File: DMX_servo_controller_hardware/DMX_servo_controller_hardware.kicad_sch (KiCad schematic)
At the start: 43 parts, among them J1 Power connector, J10 Conn_01x03, J11 Conn_01x03, J12 Conn_01x03, J2 XLR, J3 Display, J4 Rotary encoder, J5 Conn_01x03, J6 Conn_01x03, J7 Conn_01x03, J8 Conn_01x03, J9 Conn_01x03, SW1 Reset, U1 PCA9685PW, U2 SN65HVD11HD, U3 6N137, U4 Pico

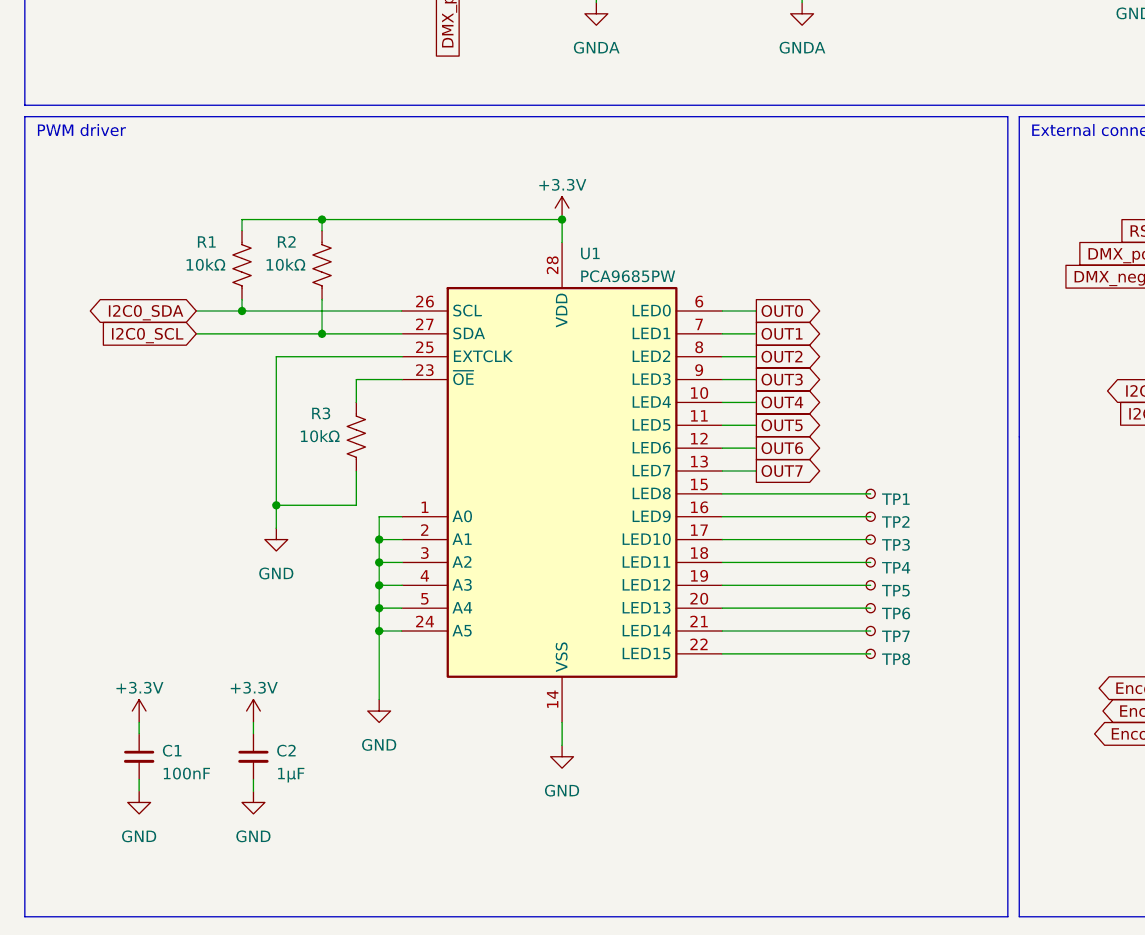
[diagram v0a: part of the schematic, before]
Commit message: Powers PCA9685 from 5V rail
With this, the PWM signal will be on the level the servos expect, since
they will be powered with the same voltage. The i2c lines are level
shifted since the RP2040 GPIOs are not 5V tolerant.
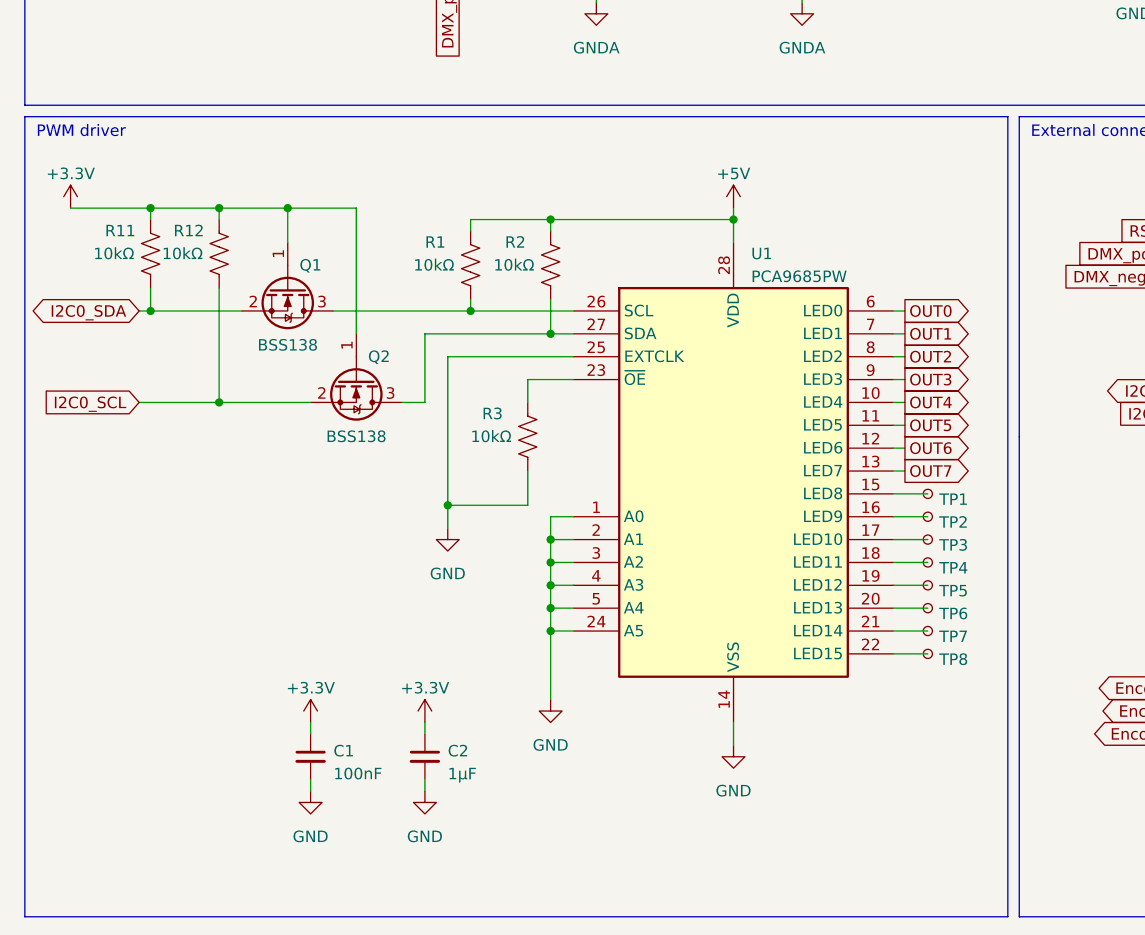
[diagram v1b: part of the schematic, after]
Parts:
- added Q1, Q2: BSS138, Package_TO_SOT_SMD:SOT-23, symbol Transistor_FET:BSS138
- added R11, R12: 10kΩ, symbol Device:R_US
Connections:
- net +3.3V: now also Q1.1 (G), Q2.1 (G), R11.1, R12.1; no longer R1.1, R2.1, U1.28 (VDD)
- net +5V: now also R1.1, R2.1, U1.28 (VDD)
- net I2C0_SCL: now also Q2.2 (S), R12.2; no longer R2.2, U1.27 (SDA)
- net I2C0_SDA: now also Q1.2 (S), R11.2; no longer R1.2, U1.26 (SCL)
- new net: Q1.3 (D), R1.2, U1.26 (SCL)
- new net: Q2.3 (D), R2.2, U1.27 (SDA)
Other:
- moved on the sheet: C1, C2, R1, R2, R3, TP1, TP2, TP3, TP4, TP5, TP6, TP7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

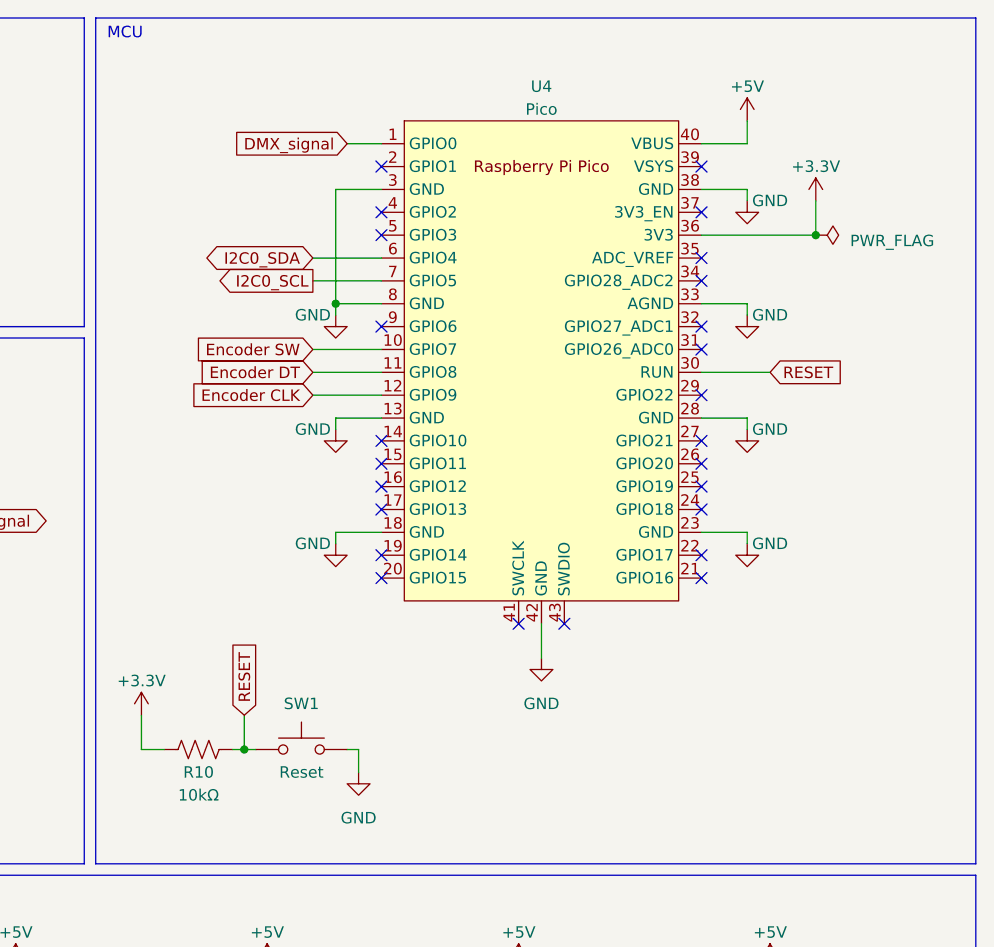
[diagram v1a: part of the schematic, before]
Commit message: Adds a diode to stop the USB from feeding the power supply when programming
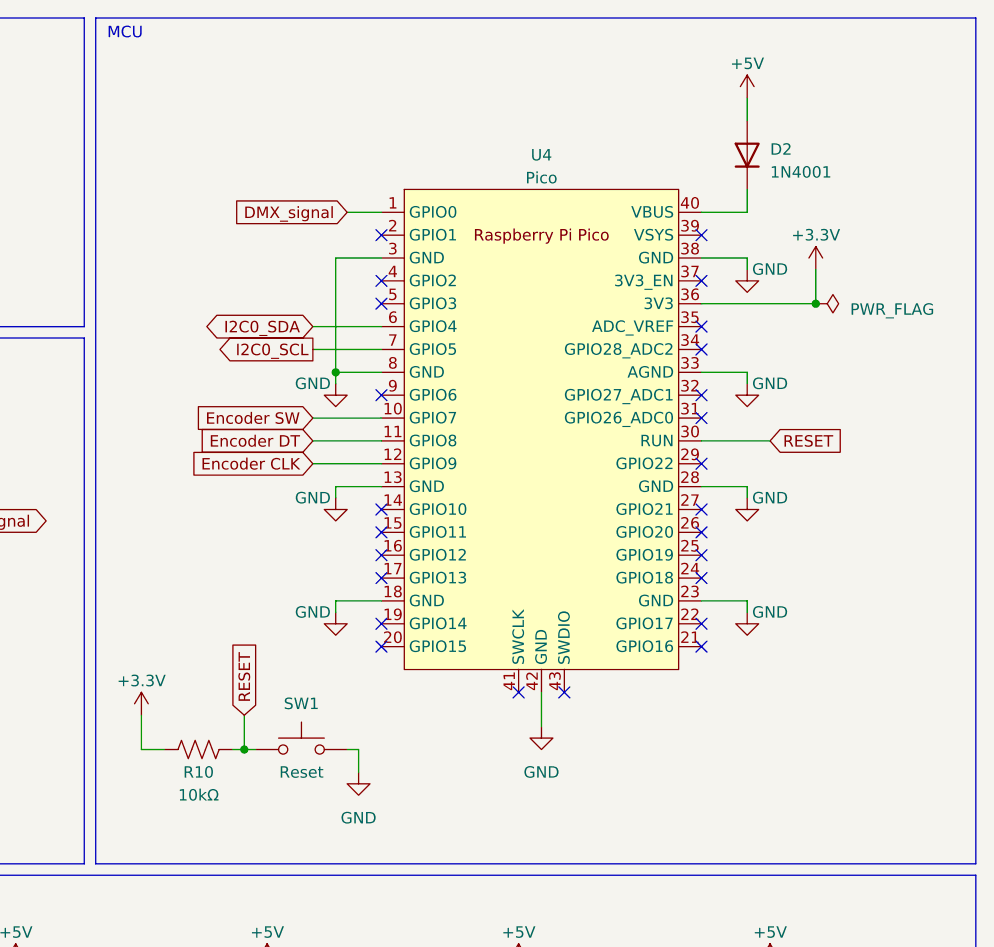
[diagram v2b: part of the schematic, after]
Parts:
- added D2: 1N4001, Diode_THT:D_DO-41_SOD81_P10.16mm_Horizontal, symbol Diode:1N4001
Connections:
- net +5V: now also D2.2 (A); no longer U4.40 (VBUS)
- new net: D2.1 (K), U4.40 (VBUS)
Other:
- moved on the sheet: U4

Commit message: Reasigns component designators
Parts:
- renumbered D2 to D1, R11 to R1, R8 to R10, R9 to R11, R10 to R12, R12 to R2, R1 to R3, R3 to R6, R2 to R7, R6 to R8, R7 to R9

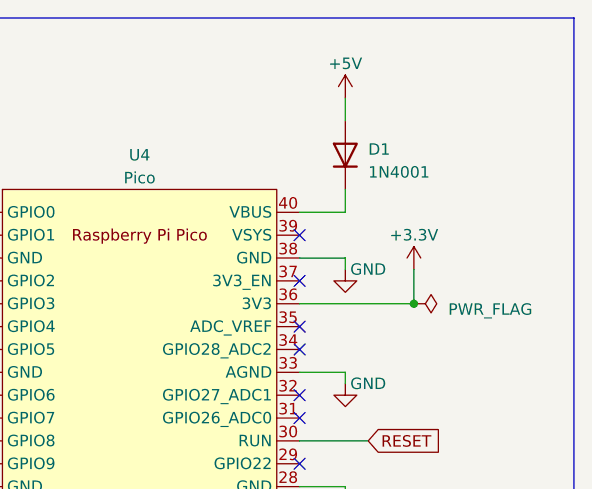
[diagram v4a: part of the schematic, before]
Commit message: Adds power flag to the VUSB net after the diode
This is necessary so the ERC will not complain about the pin do being
driven.
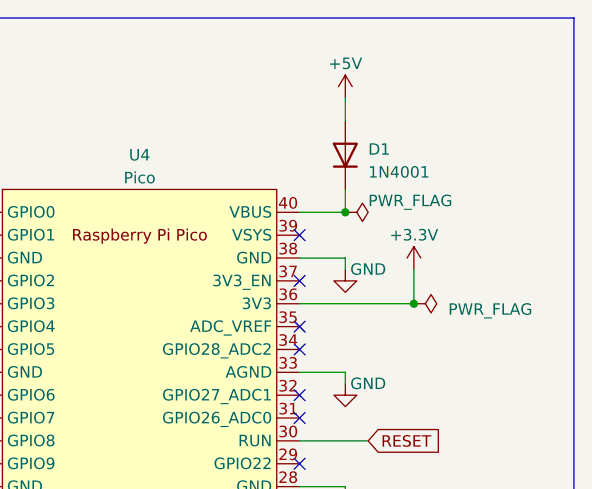
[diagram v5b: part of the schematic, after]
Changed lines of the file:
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@@
   (junction (at 71.12 160.02) (diameter 0) (color 0 0 0 0)
+  )
+  (junction (at 259.08 34.29) (diameter 0) (color 0 0 0 0)
   )
   (junction (at 62.23 129.54) (diameter 0) (color 0 0 0 0)
@@
         )
       )
+    )
+  )
+  (symbol (lib_id "power:PWR_FLAG") (at 259.08 34.29 270) (unit 1)
+    (in_bom yes) (on_board yes) (dnp no)
+    (property "Reference" "#FLG04" (at 260.985 34.29 0)
+      (effects (font (size 1.27 1.27)) hide)
+    )
+    (property "Value" "PWR_FLAG" (at 261.62 33.02 90)
+      (effects (font (size 1.27 1.27)) (justify left))
+    )
+    (property "Footprint" "" (at 259.08 34.29 0)
+      (effects (font (size 1.27 1.27)) hide)
+    )
+    (property "Datasheet" "~" (at 259.08 34.29 0)
+      (effects (font (size 1.27 1.27)) hide)
+    )
+    (pin "1")
+    (instances
+      (project "DMX_servo_controller_hardware"
+        (path "/cd90393c-7fb4-4867-84b8-7df1a2bf6613"
+          (reference "#FLG04") (unit 1)
+        )
+      )

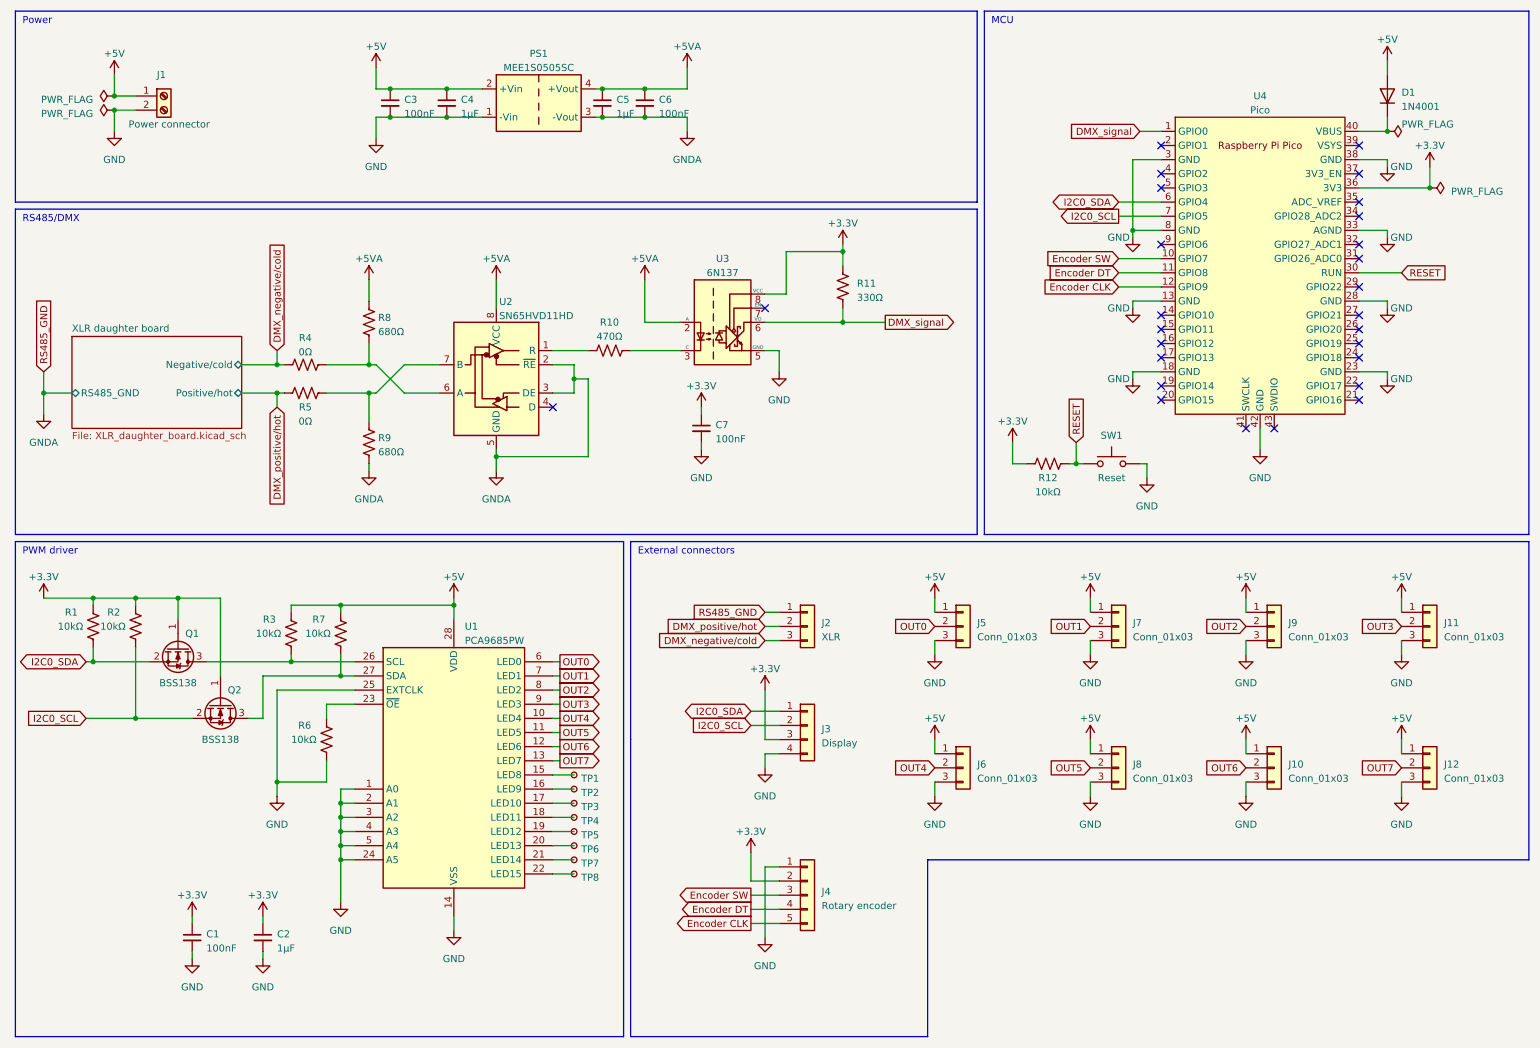
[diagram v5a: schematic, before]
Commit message: Final review of the schematics
* Fixes SCL pull-up in PCA9685
* Reviews pinouts
* Adds series resistor to PWM signals
* Adds bulk decoupling capacitor to 5V power rail
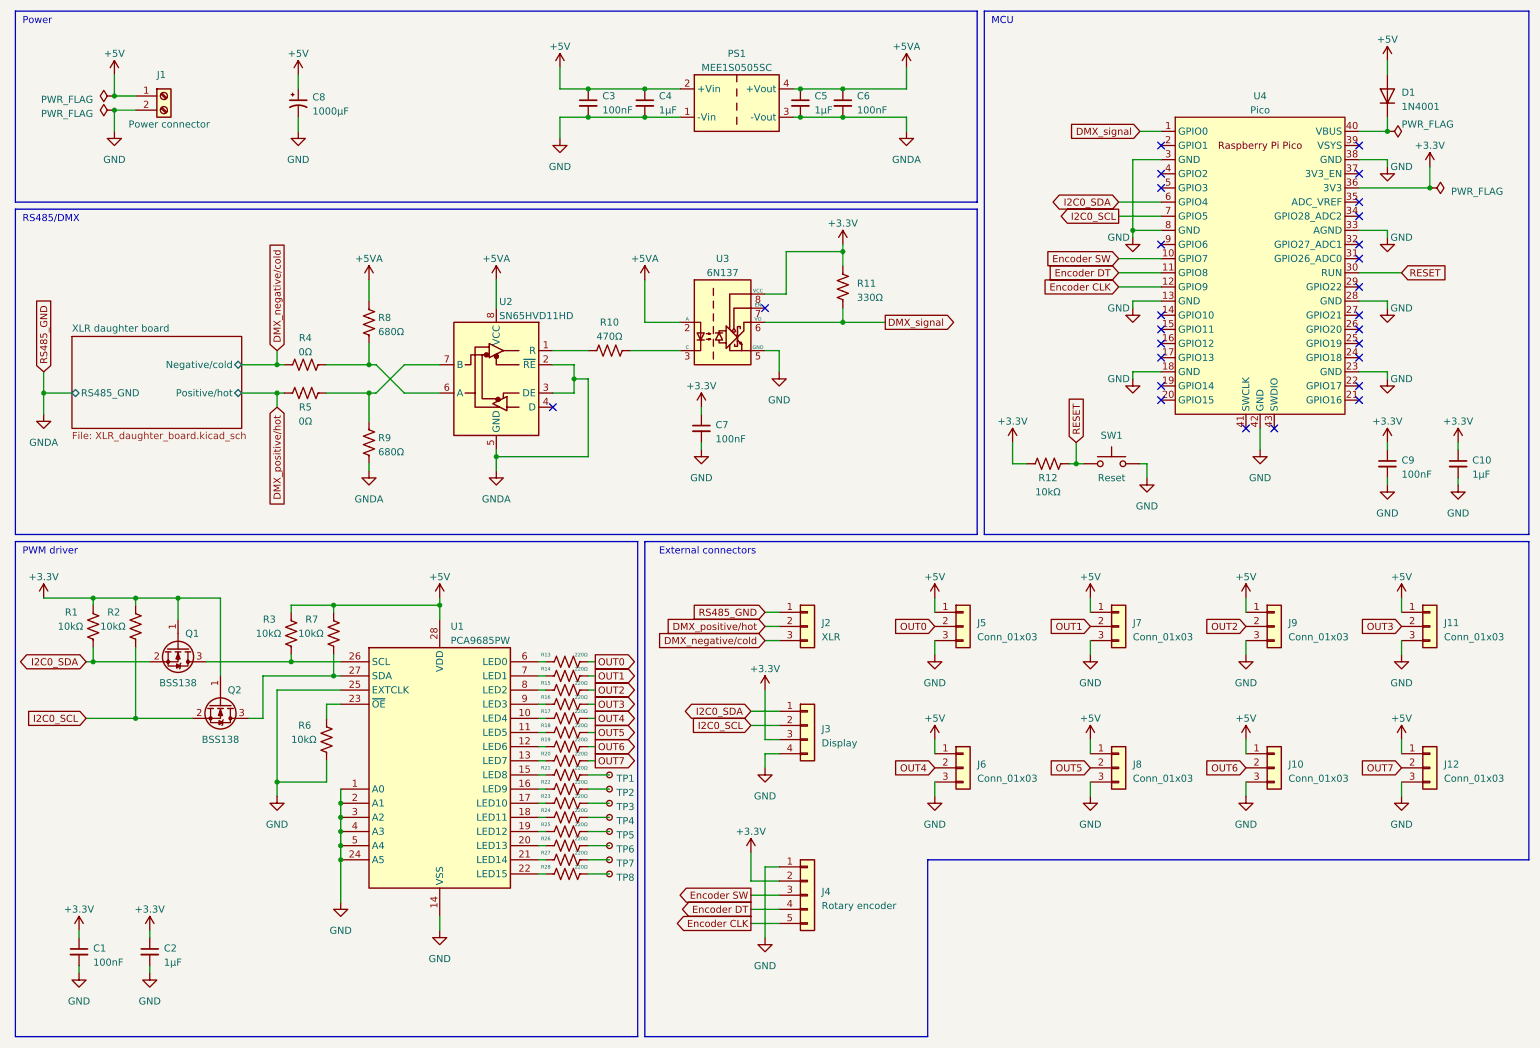
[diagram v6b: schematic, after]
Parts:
- added C10: 1μF, symbol Device:C_Small
- added C8: 1000μF, symbol Device:C_Polarized_Small_US
- added C9: 100nF, symbol Device:C_Small
- added R13, R14, R15, R16, R17, R18, R19, R20, R21, R22, R23, R24, R25, R26, R27, R28: 220Ω, symbol Device:R_US
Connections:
- net +3.3V: now also C10.1, C9.1
- net +5V: now also C8.1
- net GND: now also C10.2, C8.2, C9.2
- net OUT0: now also R13.2; no longer U1.6 (LED0)
- net OUT1: now also R14.2; no longer U1.7 (LED1)
- net OUT2: now also R15.2; no longer U1.8 (LED2)
- net OUT3: now also R16.2; no longer U1.9 (LED3)
- net OUT4: now also R17.2; no longer U1.10 (LED4)
- net OUT5: now also R18.2; no longer U1.11 (LED5)
- net OUT6: now also R19.2; no longer U1.12 (LED6)
- net OUT7: now also R20.2; no longer U1.13 (LED7)
- net at TP1.1: now also R21.2; no longer U1.15 (LED8)
- net at U1.16 (LED9): now also R22.1; no longer TP2.1
- net at U1.17 (LED10): now also R23.1; no longer TP3.1
- net at U1.18 (LED11): now also R24.1; no longer TP4.1
- net at U1.19 (LED12): now also R25.1; no longer TP5.1
- net at U1.20 (LED13): now also R26.1; no longer TP6.1
- net at U1.21 (LED14): now also R27.1; no longer TP7.1
- net at U1.22 (LED15): now also R28.1; no longer TP8.1
- new net: R27.2, TP7.1
- new net: R26.2, TP6.1
- new net: R28.2, TP8.1
- new net: R15.1, U1.8 (LED2)
- new net: R17.1, U1.10 (LED4)
- new net: R18.1, U1.11 (LED5)
- new net: R19.1, U1.12 (LED6)
- new net: R20.1, U1.13 (LED7)
- new net: R21.1, U1.15 (LED8)
- new net: R13.1, U1.6 (LED0)
- new net: R14.1, U1.7 (LED1)
- new net: R16.1, U1.9 (LED3)
- new net: R24.2, TP4.1
- new net: R25.2, TP5.1
- new net: R22.2, TP2.1
- new net: R23.2, TP3.1
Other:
- moved on the sheet: C1, C2, C3, C4, C5, C6, PS1, R7, TP1, TP2, TP3, TP4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

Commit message: Assigns footprints to some of the components
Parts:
- C1, C10, C2, C3, C4, C5, C6, C7, C9: footprint (none) -> Capacitor_SMD:C_0805_2012Metric_Pad1.18x1.45mm_HandSolder
- C8: footprint (none) -> Capacitor_THT:CP_Radial_D10.0mm_P5.00mm
- J1: footprint (none) -> TerminalBlock:TerminalBlock_bornier-2_P5.08mm
- J10, J11, J12, J5, J6, J7, J8, J9: footprint (none) -> Connector_JST:JST_XH_B3B-XH-AM_1x03_P2.50mm_Vertical
- J3: footprint (none) -> Connector_JST:JST_XH_B4B-XH-AM_1x04_P2.50mm_Vertical
- J4: footprint (none) -> Connector_JST:JST_XH_B5B-XH-AM_1x05_P2.50mm_Vertical
- R1, R10, R11, R12, R13, R14, R15, R16, R17, R18, R19, R2, R20, R21, R22, R23, R24, R25, R26, R27, R28, R3, R4, R5, R6, R7, R8, R9: footprint (none) -> Resistor_SMD:R_0815_2038Metric_Pad1.20x4.05mm_HandSolder
